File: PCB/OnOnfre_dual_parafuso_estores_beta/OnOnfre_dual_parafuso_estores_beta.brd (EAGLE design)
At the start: 44.4 x 47.7 mm, 41 parts, among them IC4 HLW8012, J7 8p, Q3 2N7002, Q4 2N7002, U2 esp12

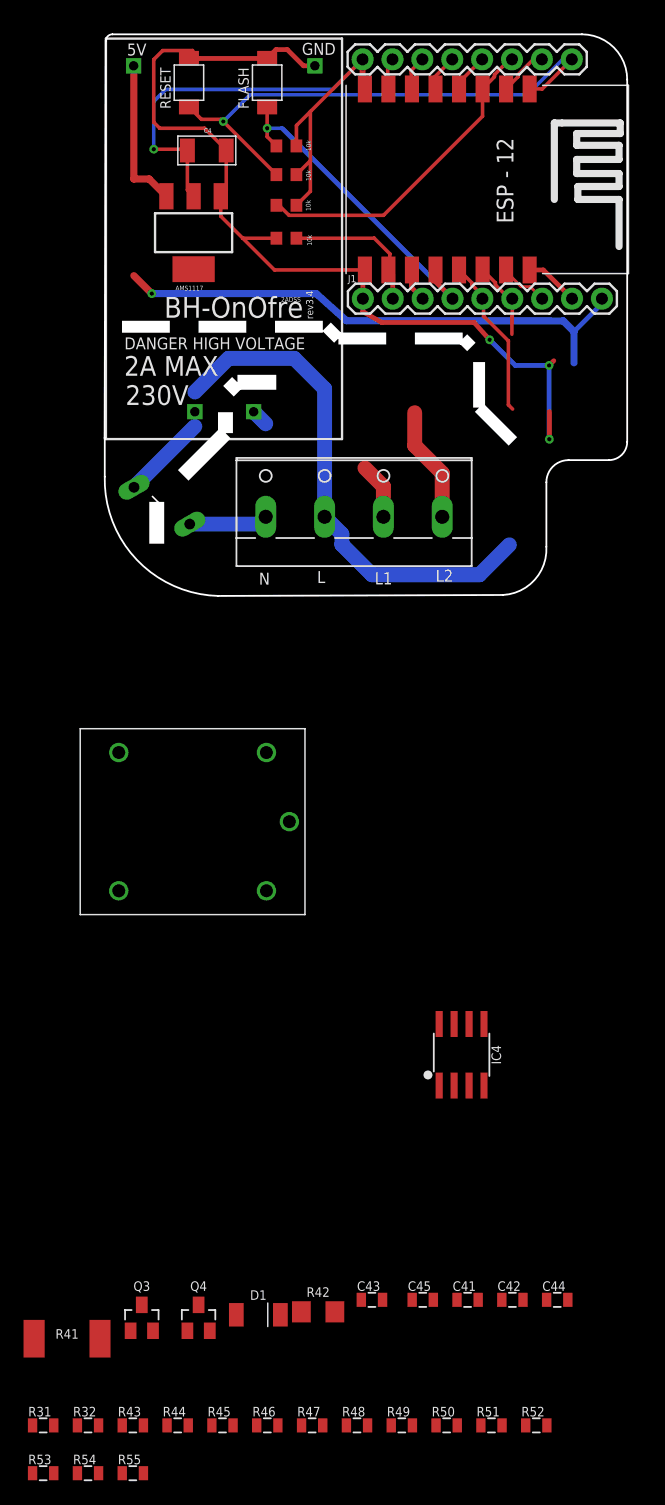
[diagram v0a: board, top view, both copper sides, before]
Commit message: estores e tomada em progresso
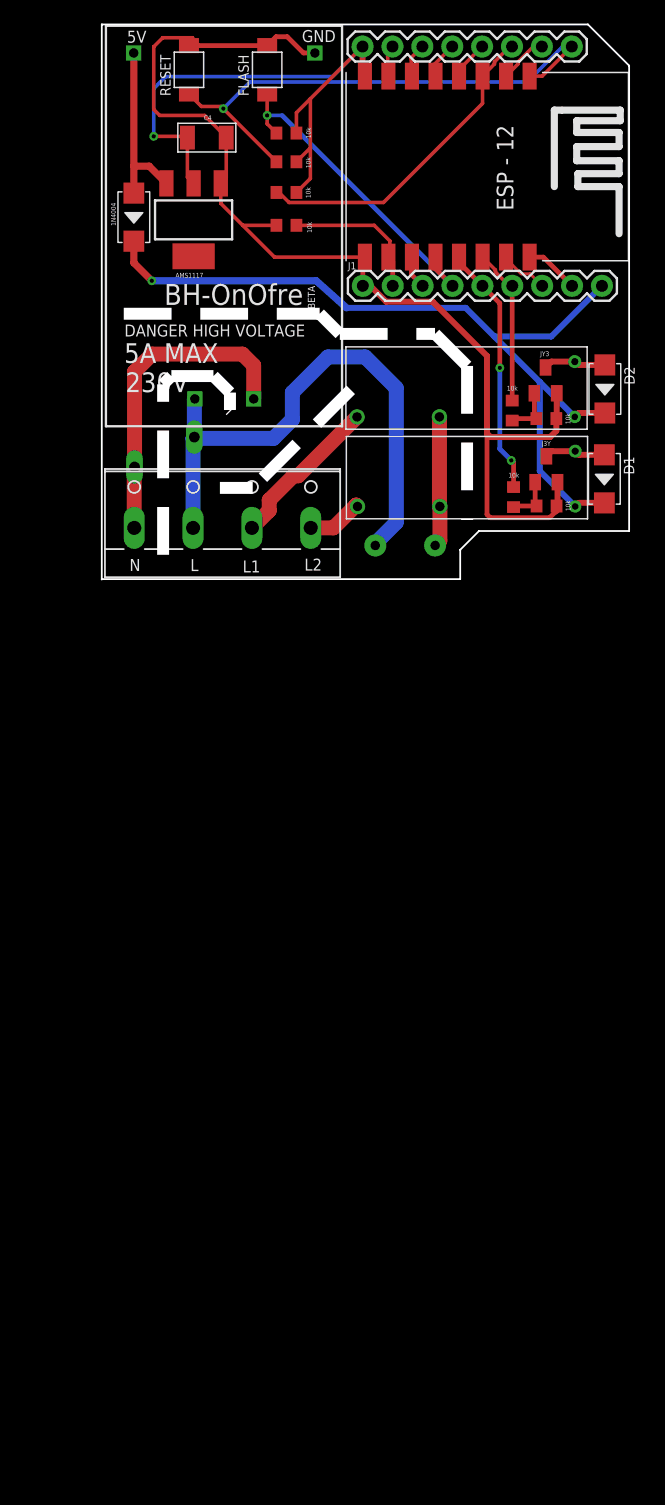
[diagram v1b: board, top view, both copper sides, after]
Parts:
- removed C41, C42: 33nF, xose:0805
- removed C43, C45: 100nF, xose:0805
- removed C44: 1uF, xose:0805
- removed IC4: HLW8012, xose:SOP8
- removed Q3, Q4: 2N7002, xose:SOT23
- removed R31, R43, R44, R50: 1K, xose:0805
- removed R32, R45, R47, R49: 10K, xose:0805
- removed R41: 0.001R, xose:2512
- removed R42: 0R, xose:1206
- removed R46, R48: 15K, xose:0805
- removed R51, R52, R53, R54, R55: 470K, xose:0805
- removed RLY1: SRD-05VDC-SL-C, Spark:SRD-5VDC-SL-C
- added D2: 1N4007, Seeed-Diode:DO-214AC
- added D3: 1N4004, Seeed-Diode:DO-214AC
- added F1: FUSE 2A, SparkFun-Fuses:PTH
- added J3Y, JY3: S8050, semicon-smd-ipc:SOT23
- added R1, R2, R3, R4: 10k, resistor:R0603
- added U$1, U$3: HF46F, HF46F:HF46F
- D1: value 1N4148 -> 1N4007; device xose:SOD80 -> Seeed-Diode:DO-214AC
- moved D1 76.9 mm to (42.9, 8.56), turned to 270 degrees
- moved X1 11.2 mm to (10.4, 5.66)
- moved R5 4.56 mm to (5.48, 10.8), turned to 90 degrees
- moved C4 1.09 mm to (9.08, 37.6)
- moved FLASH 1.09 mm to (14.2, 43.3)
- moved R8 1.09 mm to (15.8, 37.9)
- moved RESET 1.09 mm to (7.56, 43.3)
- moved AMS1117 1.09 mm to (7.96, 30.6)
- moved J1 1.09 mm to (22.3, 25.0)
- moved R11 1.09 mm to (15.8, 30.1)
- moved R9 1.09 mm to (15.8, 32.9)
- moved U$2 1.09 mm to (10.6, 30.1)
- moved J7 1.09 mm to (22.3, 45.3)
- moved R10 1.09 mm to (15.8, 35.5)
- moved U2 1.09 mm to (30.7, 35.0)
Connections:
- removed net GPIO5: Q4.1
- removed net LINE_IN: R41.2, R43.2, R5.1, U$2.P$1, X1.1
- removed net LINE_R: R41.1, R42.2, R44.2, RLY1.COMMON
- removed net N$10: IC4.8, Q4.3, R49.1
- removed net N$11: IC4.7, R45.2
- removed net N$12: C41.2, IC4.2, R43.1
- removed net N$14: C42.2, IC4.3, R44.1
- removed net N$15: R53.1, R54.1
- removed net N$16: R54.2, R55.2
- removed net N$2: IC4.6, R47.2
- removed net N$4: D1.1, Q3.3, RLY1.COIL2
- removed net N$5: Q3.1, R31.2, R32.2
- removed net N$6: R51.1, R52.1
- removed net N$8: R52.2, R53.2
- removed net NC: RLY1.CLOSED, X1.4
- removed net NO: RLY1.OPEN, X1.3
- removed net V2P: C45.2, IC4.4, R50.2, R55.1
- new net FASE_IN: R5.1, U$2.P$1, X1.1
- new net N$1: D1.1, J3Y.3, U$1.C2
- new net N$13: JY3.1, R1.2, R2.2
- new net N$7: J3Y.1, R3.2, R4.2
- new net N$9: D2.1, JY3.3, U$3.C2
- new net NEUTRAL_IN_FUSED: F1.P$2, U$1.L2, U$3.L2
- new net NEUTRAL_ONE_OUT: U$3.L1, X1.3
- new net NEUTRAL_TWO_OUT: U$1.L1, X1.4
- net 5V: now also D2.2, D3.2, U$1.C1, U$3.C1; no longer C43.2, C44.2, IC4.1, R49.2, RLY1.COIL1
- net GND: now also J3Y.2, JY3.2, R2.1, R3.1; no longer C41.1, C42.1, C43.1, C44.1, C45.1, IC4.5, Q3.2, Q4.2, R32.1, R42.1, R46.1, R48.1, R50.1
- net GPIO04: now also R4.1
- net GPIO05: now also R1.1
- net GPIO12: no longer R31.1
- net GPIO13: no longer R45.1, R46.2
- net GPIO14: no longer R47.1, R48.2
- net NEUTRAL_IN: now also F1.P$1; no longer R51.2
- net VCC: now also D3.1
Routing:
- net FASE_IN: track 0.00 -> 27.3 mm
- net 5V: track 45.7 -> 72.7 mm
- net GND: track 81.8 -> 99.5 mm, vias 3 -> 0
- net NEUTRAL_ONE_OUT: track 0.00 -> 13.4 mm
- net NEUTRAL_IN_FUSED: track 0.00 -> 11.1 mm
- net NC: track 9.81 -> 0.00 mm
- net GPIO04: track 13.9 -> 21.5 mm, vias 0 -> 2
- net LINE_IN: track 7.28 -> 0.00 mm
- net GPIO05: track 6.68 -> 13.4 mm
- net N$9: track 0.00 -> 5.36 mm
- net N$1: track 0.00 -> 5.24 mm
- net NEUTRAL_TWO_OUT: track 0.00 -> 4.82 mm
- net NO: track 4.80 -> 0.00 mm
- net N$13: track 0.00 -> 4.34 mm
- net N$7: track 0.00 -> 4.07 mm
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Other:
- board size 44.4 x 47.7 mm -> 44.8 x 47.2 mm
- board text added: "5A MAX"
- board text added: "BETA"
- board text removed: "2A MAX"
- board text removed: "2ADSS"
- board text removed: "rev3.4"

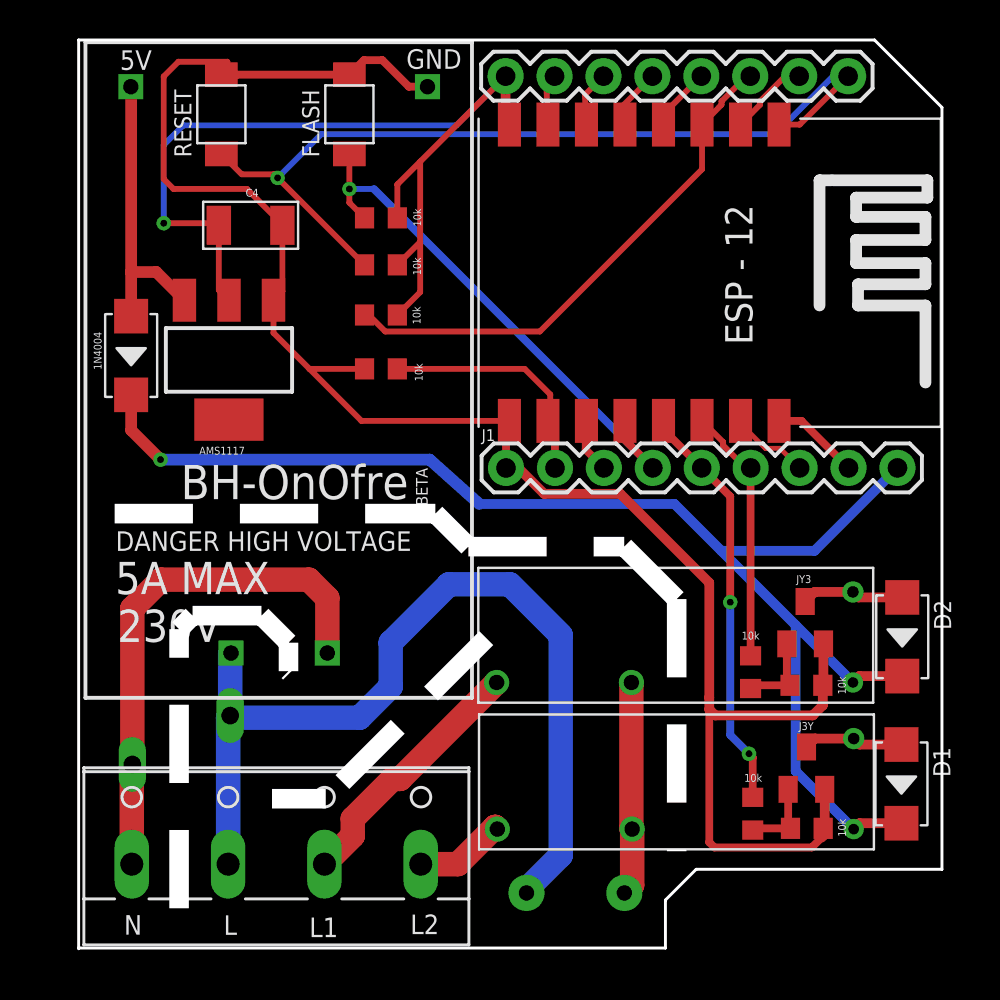
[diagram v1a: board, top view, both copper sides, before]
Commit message: remoção do OTA Arduino e adição de OTA via Web
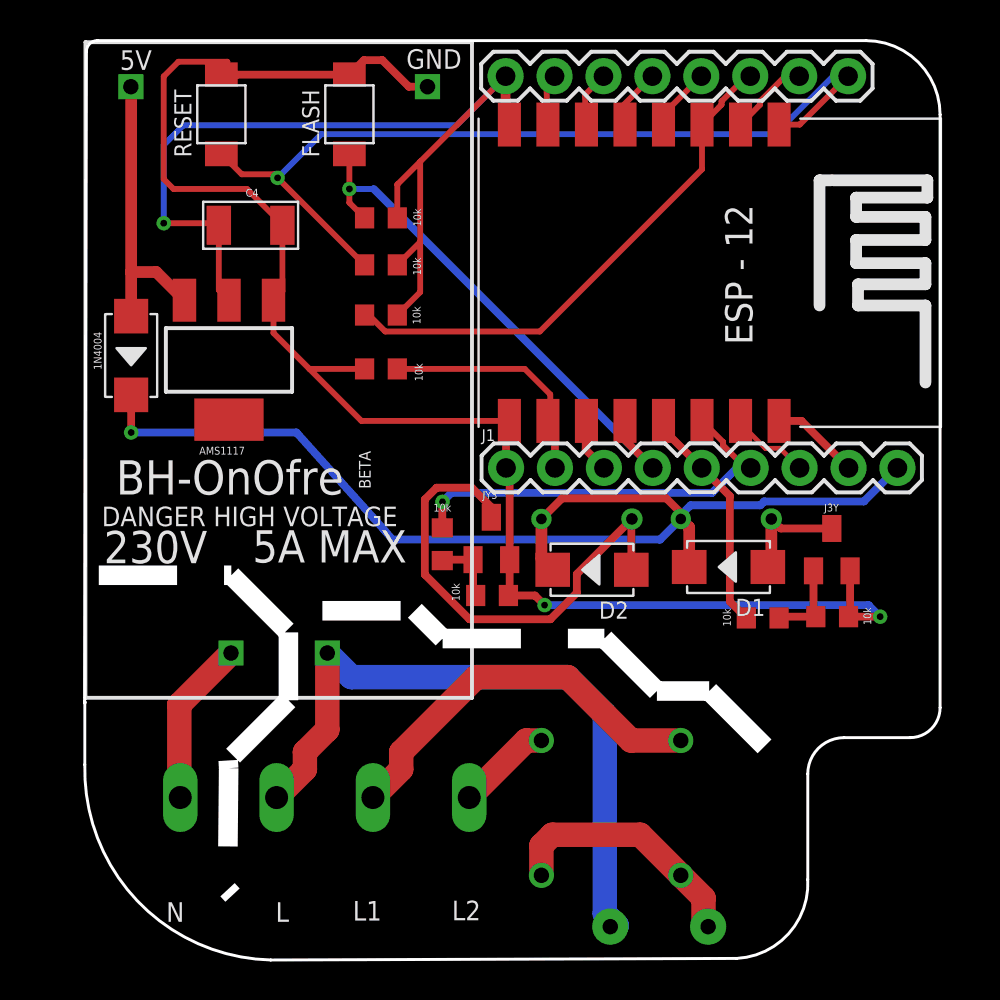
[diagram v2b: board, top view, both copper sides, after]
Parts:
- removed R5: VARISTORS07K230, varistor:S07K230
- moved U$1 21.3 mm to (30.4, 23.4), flipped to the bottom, turned to 180 degrees
- moved U$3 21.1 mm to (23.1, 23.4), flipped to the bottom, turned to 180 degrees
- moved R1 17.3 mm to (19.0, 21.0)
- moved R2 17.0 mm to (21.6, 18.3)
- moved JY3 16.9 mm to (21.6, 21.3)
- moved D2 16.5 mm to (26.8, 19.7), turned to 180 degrees
- moved D1 14.4 mm to (33.9, 19.8), turned to 180 degrees
- moved J3Y 11.4 mm to (39.3, 20.7)
- moved R3 11.1 mm to (39.3, 17.2)
- moved R4 10.2 mm to (35.7, 17.2), turned to 0 degrees
- moved F1 4.69 mm to (30.3, 1.15)
- moved X1 2.68 mm to (12.9, 6.58), flipped to the bottom, turned to 180 degrees
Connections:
- removed net FASE_IN: R5.1, U$2.P$1, X1.1
- new net LINE_IN: U$2.P$2, X1.1
- net NEUTRAL_IN: now also U$2.P$1; no longer R5.2, U$2.P$2
- net NEUTRAL_IN_FUSED: now also U$1.L1, U$3.L1; no longer U$1.L2, U$3.L2
- net NEUTRAL_ONE_OUT: now also U$1.L2; no longer U$3.L1
- net NEUTRAL_TWO_OUT: now also U$3.L2; no longer U$1.L1
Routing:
- net FASE_IN: track 27.3 -> 0.00 mm
- net N$9: track 5.36 -> 25.6 mm
- net GND: track 99.5 -> 84.6 mm, vias 0 -> 2
- net 5V: track 72.7 -> 59.7 mm
- net NEUTRAL_IN: track 47.7 -> 35.9 mm
- net GPIO04: track 21.5 -> 12.0 mm, vias 2 -> 0
- net LINE_IN: track 0.00 -> 9.37 mm
- net GPIO05: track 13.4 -> 21.7 mm, vias 0 -> 1
- net NEUTRAL_ONE_OUT: track 13.4 -> 20.5 mm
- net NEUTRAL_IN_FUSED: track 11.1 -> 13.2 mm
- net N$13: track 4.34 -> 3.53 mm
- net N$1: track 5.24 -> 5.91 mm
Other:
- board size 44.8 x 47.2 mm -> 44.4 x 47.7 mm
